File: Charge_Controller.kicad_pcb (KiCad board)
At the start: 2 copper layers, 127 x 73.7 mm, 137 parts, among them J1 SOLAR, J10 Conn_01x01_Female, J11 Conn_01x01_Female, J12 Conn_01x01_Female, J13 Conn_01x01_Female, J14 Conn_01x01_Female, J15 Conn_01x01_Female, J16 Conn_01x01_Female, J17 Conn_01x01_Female, J18 Conn_01x01_Female, J19 Conn_01x01_Female, J2 Conn_01x01_Female, J20 Conn_01x01_Female, J21 Conn_01x01_Female, J22 Conn_01x01_Female, J23 Conn_01x01_Female, J24 Conn_01x01_Female, J25 Conn_01x01_Female, J26 Conn_01x01_Female, J27 Conn_01x01_Female, J28 Conn_01x01_Female, J29 Conn_01x01_Female, J3 Conn_01x01_Female, J30 Conn_01x01_Female, J31 Conn_01x01_Female, J32 Conn_01x01_Female, J33 SOLAR, J34 BATT, J4 Conn_01x01_Female, J5 Conn_01x01_Female, J6 Conn_01x01_Female, J7 Conn_01x01_Female, J8 BATT, J9 USB_OTG, Q1 CSD19505, Q2 CSD19505, Q3 CSD19505, Q4 Si2306, Q5 2N3904, Q6 2N3904, Q7 PMOS-100V-90A, Q8 PMOS-100V-90A, U1 ACS712-30A, U10 ADS1015, U11 NUP4202, U2 B1212, U3 AMS1117-5.0, U4 AMS1117-3.3, U5 XL7005A, U6 XL7005A, U7 IR2104, U8 ESP32-WROOM-32, U9 CH340G

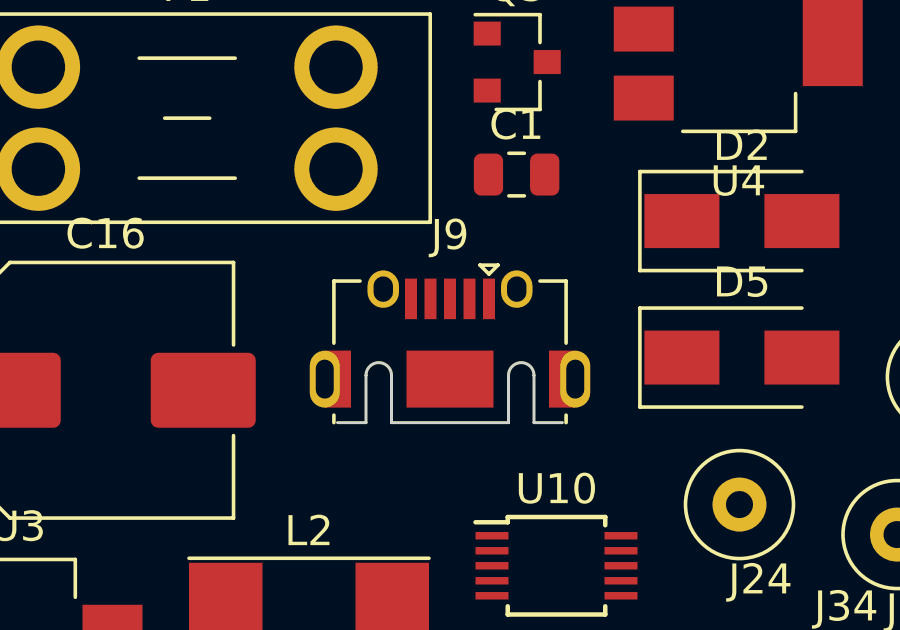
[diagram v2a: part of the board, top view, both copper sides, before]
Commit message: Added FAN controller circuit
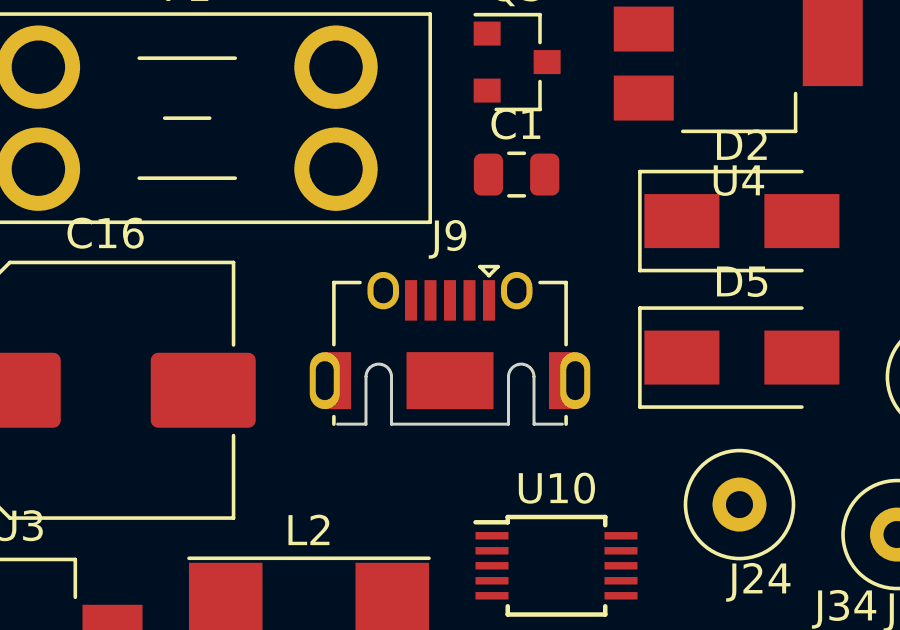
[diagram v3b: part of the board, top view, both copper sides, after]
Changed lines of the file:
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@@
     (tags "Micro AB USB SMD")
     (attr smd)
-    (fp_text reference J9 (at 0 -3.4014 -180) (layer F.SilkS)
+    (fp_text reference J9 (at 0 -3.3514 -180) (layer F.SilkS)
       (effects (font (size 1 1) (thickness 0.15)))
     )
-    (fp_text value USB_OTG (at 0 4.8986) (layer F.Fab)
+    (fp_text value USB_OTG (at 0 4.9486) (layer F.Fab)
       (effects (font (size 1 1) (thickness 0.15)))
     )
-    (fp_line (start -3.75 2.8486) (end 3.75 2.8486) (layer F.Fab) (width 0.1))
-    (fp_text user "PCB Edge" (at 0 2.8486) (layer Dwgs.User)
+    (fp_line (start -3.75 2.8986) (end 3.75 2.8986) (layer F.Fab) (width 0.1))
+    (fp_text user "PCB Edge" (at 0 2.8986) (layer Dwgs.User)
       (effects (font (size 0.4 0.4) (thickness 0.04)))
     )
-    (fp_text user %R (at 0 -0.1014) (layer F.Fab)
+    (fp_text user %R (at 0 -0.0514) (layer F.Fab)
       (effects (font (size 1 1) (thickness 0.15)))
     )
-    (fp_line (start -3.87 2.5986) (end -3.87 2.8486) (layer F.SilkS) (width 0.12))
-    (fp_line (start 3.87 2.5986) (end 3.87 2.8486) (layer F.SilkS) (width 0.12))
-    (fp_line (start 3 -1.8714) (end 3.87 -1.8714) (layer F.SilkS) (width 0.12))
-    (fp_line (start -3.87 -1.8714) (end -3.87 0.1986) (layer F.SilkS) (width 0.12))
-    (fp_line (start 3.87 -1.8714) (end 3.87 0.1986) (layer F.SilkS) (width 0.12))
-    (fp_line (start -3.75 3.5486) (end 3.75 3.5486) (layer F.Fab) (width 0.1))
-    (fp_line (start -3.75 -1.7514) (end -3.75 2.8486) (layer F.Fab) (width 0.1))
-    (fp_line (start -3.75 2.8486) (end -2.8 2.8486) (layer Edge.Cuts) (width 0.1))
-    (fp_line (start -2.8 1.2736) (end -2.8 2.8486) (layer Edge.Cuts) (width 0.1))
-    (fp_line (start -1.95 1.2736) (end -1.95 2.8486) (layer Edge.Cuts) (width 0.1))
-    (fp_line (start -1.95 2.8486) (end 1.95 2.8486) (layer Edge.Cuts) (width 0.1))
-    (fp_line (start 1.95 1.2736) (end 1.95 2.8486) (layer Edge.Cuts) (width 0.1))
-    (fp_line (start 2.8 1.2736) (end 2.8 2.8486) (layer Edge.Cuts) (width 0.1))
-    (fp_line (start 2.8 2.8486) (end 3.75 2.8486) (layer Edge.Cuts) (width 0.1))
-    (fp_line (start 3.75 -1.7514) (end 3.75 2.8486) (layer F.Fab) (width 0.1))
-    (fp_line (start -3.75 -1.7514) (end 3.75 -1.7514) (layer F.Fab) (width 0.1))
-    (fp_line (start -5.18 -2.7314) (end 5.18 -2.7314) (layer F.CrtYd) (width 0.05))
-    (fp_line (start 5.18 -2.7314) (end 5.18 4.0486) (layer F.CrtYd) (width 0.05))
-    (fp_line (start -5.18 -2.7314) (end -5.18 4.0486) (layer F.CrtYd) (width 0.05))
-    (fp_line (start -5.18 4.0486) (end 5.18 4.0486) (layer F.CrtYd) (width 0.05))
-    (fp_arc (start -2.375 1.2736) (end -2.8 1.2736) (angle 180) (layer Edge.Cuts) (width 0.1))
-    (fp_arc (start 2.375 1.2736) (end 1.95 1.2736) (angle 180) (layer Edge.Cuts) (width 0.1))
-    (fp_line (start -3.87 -1.8714) (end -3 -1.8714) (layer F.SilkS) (width 0.12))
-    (fp_line (start 1.3 -2.1014) (end 1 -2.4014) (layer F.SilkS) (width 0.12))
-    (fp_line (start 1.3 -2.1014) (end 1.6 -2.4014) (layer F.SilkS) (width 0.12))
-    (fp_line (start 1 -2.4014) (end 1.6 -2.4014) (layer F.SilkS) (width 0.12))
-    (pad "" smd rect (at -3.5 1.3986) (size 0.3 0.85) (layers F.Paste))
-    (pad "" smd rect (at 3.5 1.3986) (size 0.3 0.85) (layers F.Paste))
-    (pad 6 smd rect (at -3.7375 1.3986) (size 0.875 1.9) (layers F.Cu F.Mask)
+    (fp_line (start -3.87 2.6486) (end -3.87 2.8986) (layer F.SilkS) (width 0.12))
+    (fp_line (start 3.87 2.6486) (end 3.87 2.8986) (layer F.SilkS) (width 0.12))
+    (fp_line (start 3 -1.8214) (end 3.87 -1.8214) (layer F.SilkS) (width 0.12))
+    (fp_line (start -3.87 -1.8214) (end -3.87 0.2486) (layer F.SilkS) (width 0.12))
+    (fp_line (start 3.87 -1.8214) (end 3.87 0.2486) (layer F.SilkS) (width 0.12))
+    (fp_line (start -3.75 3.5986) (end 3.75 3.5986) (layer F.Fab) (width 0.1))
+    (fp_line (start -3.75 -1.7014) (end -3.75 2.8986) (layer F.Fab) (width 0.1))
+    (fp_line (start -3.75 2.8986) (end -2.8 2.8986) (layer Edge.Cuts) (width 0.1))
+    (fp_line (start -2.8 1.3236) (end -2.8 2.8986) (layer Edge.Cuts) (width 0.1))
+    (fp_line (start -1.95 1.3236) (end -1.95 2.8986) (layer Edge.Cuts) (width 0.1))
+    (fp_line (start -1.95 2.8986) (end 1.95 2.8986) (layer Edge.Cuts) (width 0.1))
+    (fp_line (start 1.95 1.3236) (end 1.95 2.8986) (layer Edge.Cuts) (width 0.1))
+    (fp_line (start 2.8 1.3236) (end 2.8 2.8986) (layer Edge.Cuts) (width 0.1))
+    (fp_line (start 2.8 2.8986) (end 3.75 2.8986) (layer Edge.Cuts) (width 0.1))
+    (fp_line (start 3.75 -1.7014) (end 3.75 2.8986) (layer F.Fab) (width 0.1))
+    (fp_line (start -3.75 -1.7014) (end 3.75 -1.7014) (layer F.Fab) (width 0.1))
+    (fp_line (start -5.18 -2.6814) (end 5.18 -2.6814) (layer F.CrtYd) (width 0.05))
+    (fp_line (start 5.18 -2.6814) (end 5.18 4.0986) (layer F.CrtYd) (width 0.05))
+    (fp_line (start -5.18 -2.6814) (end -5.18 4.0986) (layer F.CrtYd) (width 0.05))
+    (fp_line (start -5.18 4.0986) (end 5.18 4.0986) (layer F.CrtYd) (width 0.05))
+    (fp_arc (start -2.375 1.3236) (end -2.8 1.3236) (angle 180) (layer Edge.Cuts) (width 0.1))
+    (fp_arc (start 2.375 1.3236) (end 1.95 1.3236) (angle 180) (layer Edge.Cuts) (width 0.1))
+    (fp_line (start -3.87 -1.8214) (end -3 -1.8214) (layer F.SilkS) (width 0.12))
+    (fp_line (start 1.3 -2.0514) (end 1 -2.3514) (layer F.SilkS) (width 0.12))
+    (fp_line (start 1.3 -2.0514) (end 1.6 -2.3514) (layer F.SilkS) (width 0.12))
+    (fp_line (start 1 -2.3514) (end 1.6 -2.3514) (layer F.SilkS) (width 0.12))
+    (pad "" smd rect (at -3.5 1.4486) (size 0.3 0.85) (layers F.Paste))
+    (pad "" smd rect (at 3.5 1.4486) (size 0.3 0.85) (layers F.Paste))
+    (pad 6 smd rect (at -3.7375 1.4486) (size 0.875 1.9) (layers F.Cu F.Mask)
       (net 24 "Net-(C25-Pad1)"))
-    (pad 6 smd rect (at 3.7375 1.3986) (size 0.875 1.9) (layers F.Cu F.Mask)
+    (pad 6 smd rect (at 3.7375 1.4486) (size 0.875 1.9) (layers F.Cu F.Mask)
       (net 24 "Net-(C25-Pad1)"))
-    (pad 6 smd rect (at 0 1.3986) (size 2.9 1.9) (layers F.Cu F.Paste F.Mask)
+    (pad 6 smd rect (at 0 1.4486) (size 2.9 1.9) (layers F.Cu F.Paste F.Mask)
       (net 24 "Net-(C25-Pad1)"))
-    (pad 2 smd rect (at 0.65 -1.2764) (size 0.4 1.35) (layers F.Cu F.Paste F.Mask)
+    (pad 2 smd rect (at 0.65 -1.2264) (size 0.4 1.35) (layers F.Cu F.Paste F.Mask)
       (net 38 "Net-(J9-Pad2)"))
-    (pad 6 thru_hole oval (at 4.175 1.3986) (size 1 1.9) (drill oval 0.6 1.3) (layers *.Cu *.Mask)
+    (pad 6 thru_hole oval (at 4.175 1.4486) (size 1 1.9) (drill oval 0.6 1.3) (layers *.Cu *.Mask)
       (net 24 "Net-(C25-Pad1)"))
-    (pad 6 thru_hole oval (at -4.175 1.3986) (size 1 1.9) (drill oval 0.6 1.3) (layers *.Cu *.Mask)
+    (pad 6 thru_hole oval (at -4.175 1.4486) (size 1 1.9) (drill oval 0.6 1.3) (layers *.Cu *.Mask)
       (net 24 "Net-(C25-Pad1)"))
-    (pad 6 thru_hole oval (at 2.225 -1.6014) (size 1.05 1.25) (drill oval 0.65 0.85) (layers *.Cu *.Mask)
+    (pad 6 thru_hole oval (at 2.225 -1.5514) (size 1.05 1.25) (drill oval 0.65 0.85) (layers *.Cu *.Mask)
       (net 24 "Net-(C25-Pad1)"))
-    (pad 1 smd rect (at 1.3 -1.2764) (size 0.4 1.35) (layers F.Cu F.Paste F.Mask)
+    (pad 1 smd rect (at 1.3 -1.2264) (size 0.4 1.35) (layers F.Cu F.Paste F.Mask)
       (net 22 /USBV))
-    (pad 3 smd rect (at 0 -1.2764) (size 0.4 1.35) (layers F.Cu F.Paste F.Mask)
+    (pad 3 smd rect (at 0 -1.2264) (size 0.4 1.35) (layers F.Cu F.Paste F.Mask)
       (net 39 "Net-(J9-Pad3)"))
-    (pad 4 smd rect (at -0.65 -1.2764) (size 0.4 1.35) (layers F.Cu F.Paste F.Mask)
+    (pad 4 smd rect (at -0.65 -1.2264) (size 0.4 1.35) (layers F.Cu F.Paste F.Mask)
       (net 40 /USBID))
-    (pad 5 smd rect (at -1.3 -1.2764) (size 0.4 1.35) (layers F.Cu F.Paste F.Mask)
+    (pad 5 smd rect (at -1.3 -1.2264) (size 0.4 1.35) (layers F.Cu F.Paste F.Mask)
       (net 1 GND))
-    (pad 6 thru_hole oval (at -2.225 -1.6014) (size 1.05 1.25) (drill oval 0.65 0.85) (layers *.Cu *.Mask)
+    (pad 6 thru_hole oval (at -2.225 -1.5514) (size 1.05 1.25) (drill oval 0.65 0.85) (layers *.Cu *.Mask)
       (net 24 "Net-(C25-Pad1)"))
     (model ${KISYS3DMOD}/Connector_USB.3dshapes/USB_Micro-AB_Molex_47590-0001.wrl

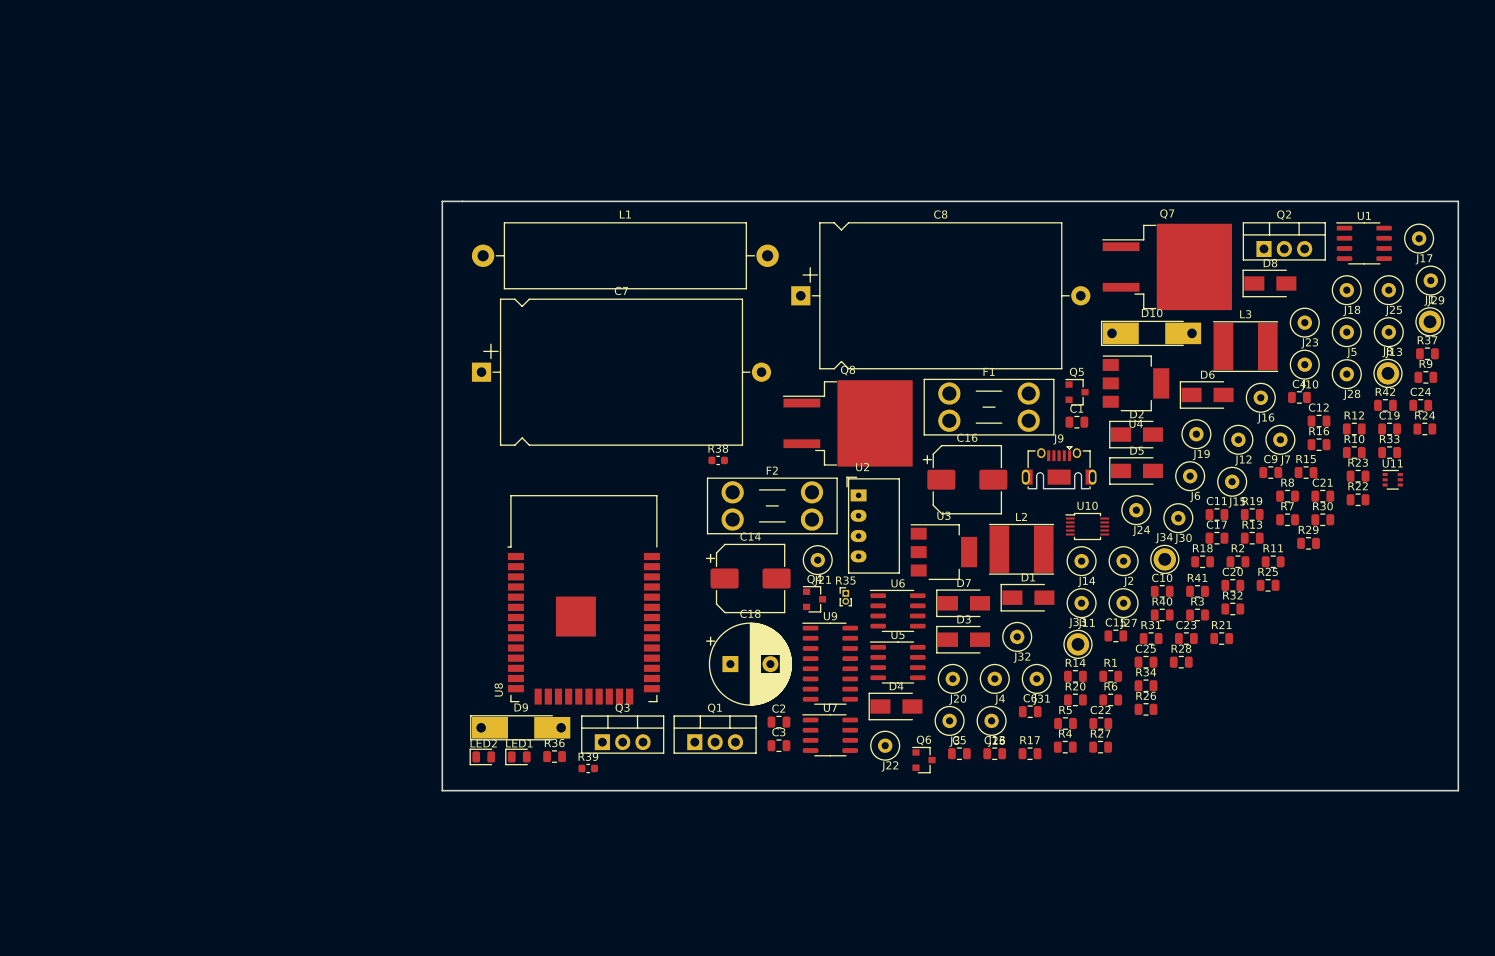
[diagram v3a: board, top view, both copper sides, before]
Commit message: Started layout of PCB, first grouping of components.
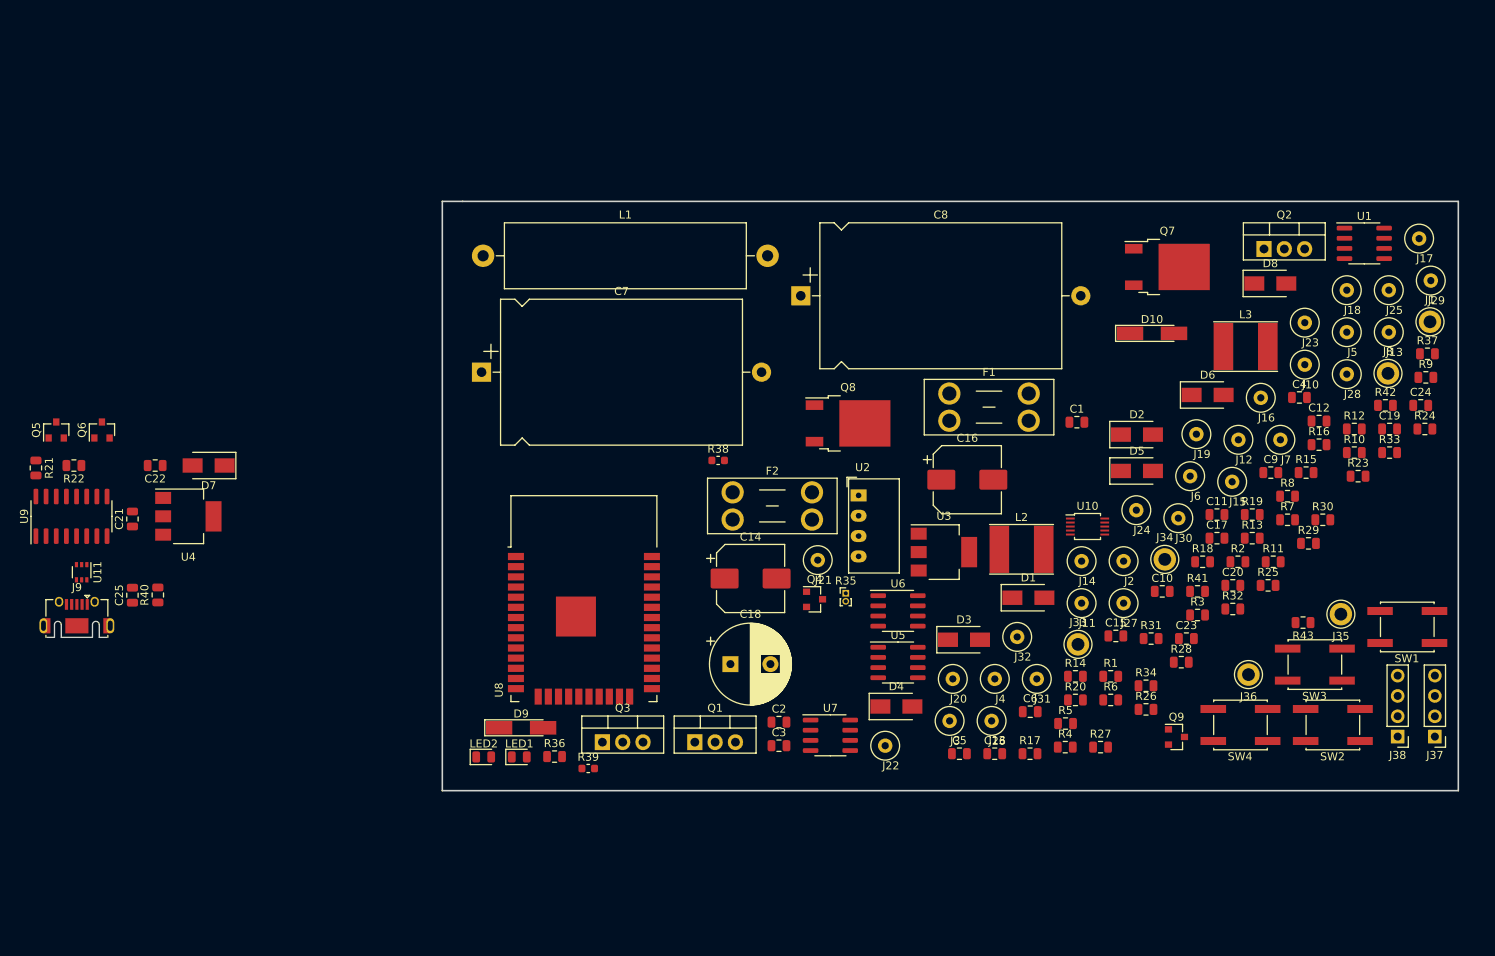
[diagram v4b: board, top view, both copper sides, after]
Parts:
- added J35: BATT, TestPoint:TestPoint_Keystone_5005-5009_Compact, F.Cu at (190.2, 113.5)
- added J36: FAN, TestPoint:TestPoint_Keystone_5005-5009_Compact, F.Cu at (178.7, 121.0)
- added J37: I2C_CON, Connector_PinHeader_2.54mm:PinHeader_1x04_P2.54mm_Vertical, F.Cu at (201.9, 128.8)
- added J38: I2C_CON, Connector_PinHeader_2.54mm:PinHeader_1x04_P2.54mm_Vertical, F.Cu at (197.3, 128.8)
- added Q9: Si2306, Package_TO_SOT_SMD:SOT-23, F.Cu at (169.7, 128.8)
- added R43: 10k, Resistor_SMD:R_0805_2012Metric, F.Cu at (185.5, 114.5)
- added SW1: RIGHT, Button_Switch_SMD:SW_SPST_EVQQ2, F.Cu at (198.5, 115.1)
- added SW2: RIGHT, Button_Switch_SMD:SW_SPST_EVQQ2, F.Cu at (189.2, 127.3)
- added SW3: RIGHT, Button_Switch_SMD:SW_SPST_EVQQ2, F.Cu at (186.9, 119.8)
- added SW4: RIGHT, Button_Switch_SMD:SW_SPST_EVQQ2, F.Cu at (177.7, 127.3)
- D10, D9: footprint Diode_SMD:D_MELF-RM10_Universal_Handsoldering -> Diode_SMD:D_MiniMELF_Handsoldering
- Q7, Q8: value PMOS-100V-90A -> PMOS-100V-78A; footprint Package_TO_SOT_SMD:TO-263-2 -> Package_TO_SOT_SMD:TO-252-2
- moved U11 164.3 mm to (32.8, 108.3), turned to 90 degrees
- moved R22 160.6 mm to (31.8, 94.9), turned to 180 degrees
- moved R21 149.7 mm to (27.1, 95.2), turned to 270 degrees
- moved C21 148.8 mm to (39.1, 101.6), turned to 90 degrees
- moved Q5 127.7 mm to (29.6, 90.5), turned to 270 degrees
- moved C25 127.0 mm to (39.1, 111.1), turned to 90 degrees
- moved R40 125.6 mm to (42.3, 111.1), turned to 90 degrees
- moved J9 124.2 mm to (32.2, 113.5)
- moved C22 122.5 mm to (42.0, 94.9), turned to 180 degrees
- moved U4 119.6 mm to (46.1, 101.3)
- moved Q6 110.7 mm to (35.3, 90.5), turned to 270 degrees
- moved U9 96.6 mm to (31.5, 101.3), turned to 0 degrees
- moved D7 96.0 mm to (48.7, 94.9), turned to 180 degrees
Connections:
- net /GPIO18 renamed /PB_LFT
- net /GPIO19 renamed /PB_BCK
- net Net-(LED1-Pad2) renamed /LED1
- net Net-(R25-Pad2) renamed /PB-SEL
- R28 pad 2: /GPIO17 -> /PB-RHT
- U11 pad 4: Net-(J9-Pad2) -> Net-(J9-Pad3)
- U8 pad 27: /GPIO17 -> /FAN-CR
- U8 pad 28: /GPIO17 -> /PB-RHT
